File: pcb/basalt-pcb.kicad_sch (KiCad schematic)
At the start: 16 parts, among them J1 Conn_01x07_Pin, J2 Conn_01x07_Pin, J3 USB4215-03-A, J4 Conn_01x04_Pin, U1 DI78L3.3ZAB, U2 STM32C071F8Px

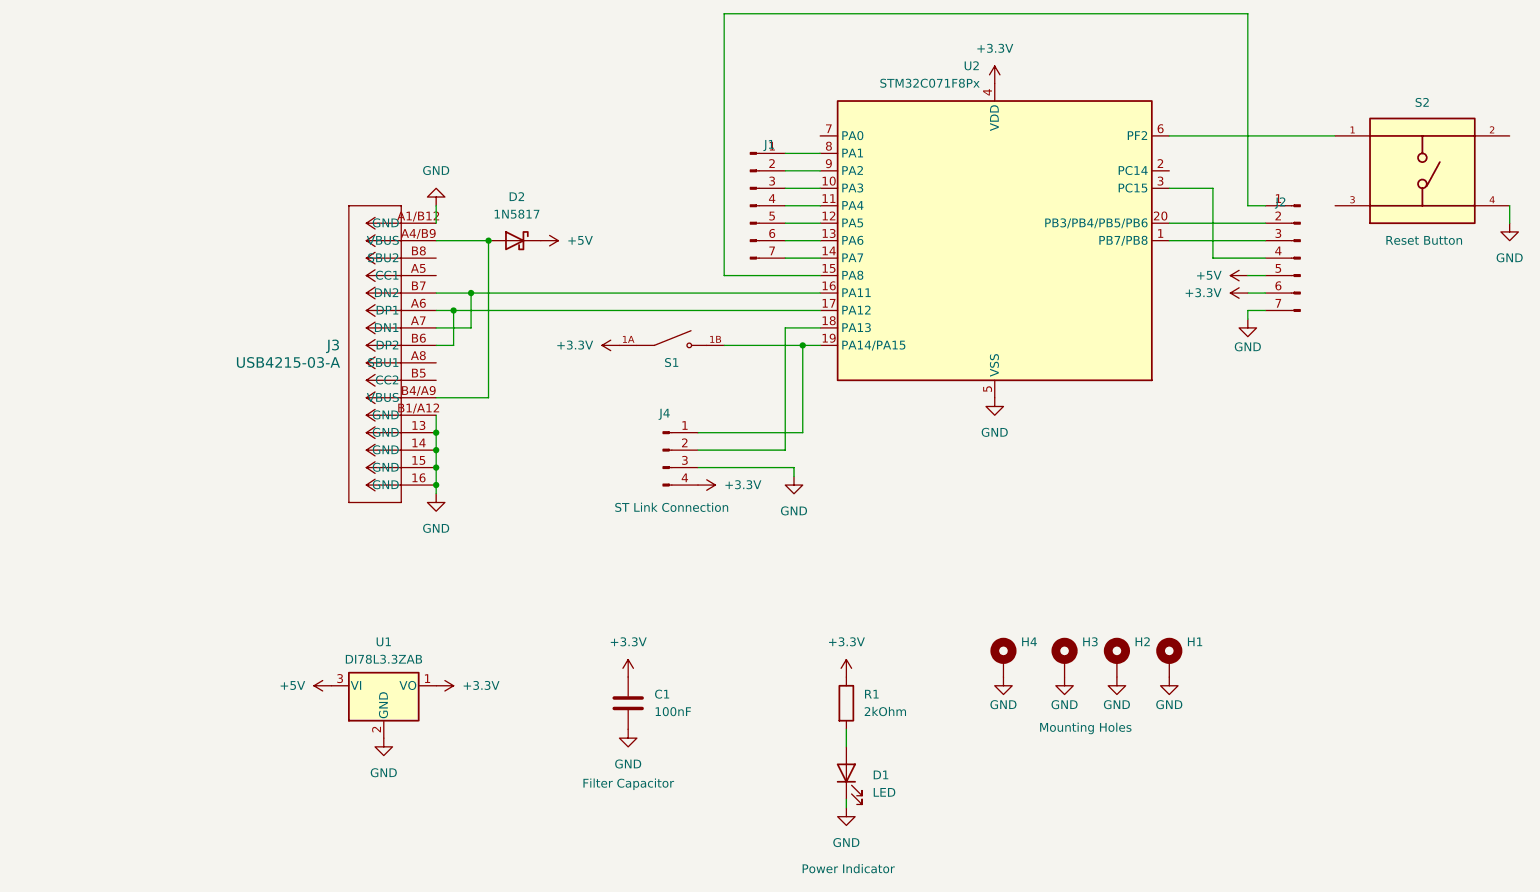
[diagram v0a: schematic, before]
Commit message: Begin work on Rev B with diode array / dedicated Vin pin
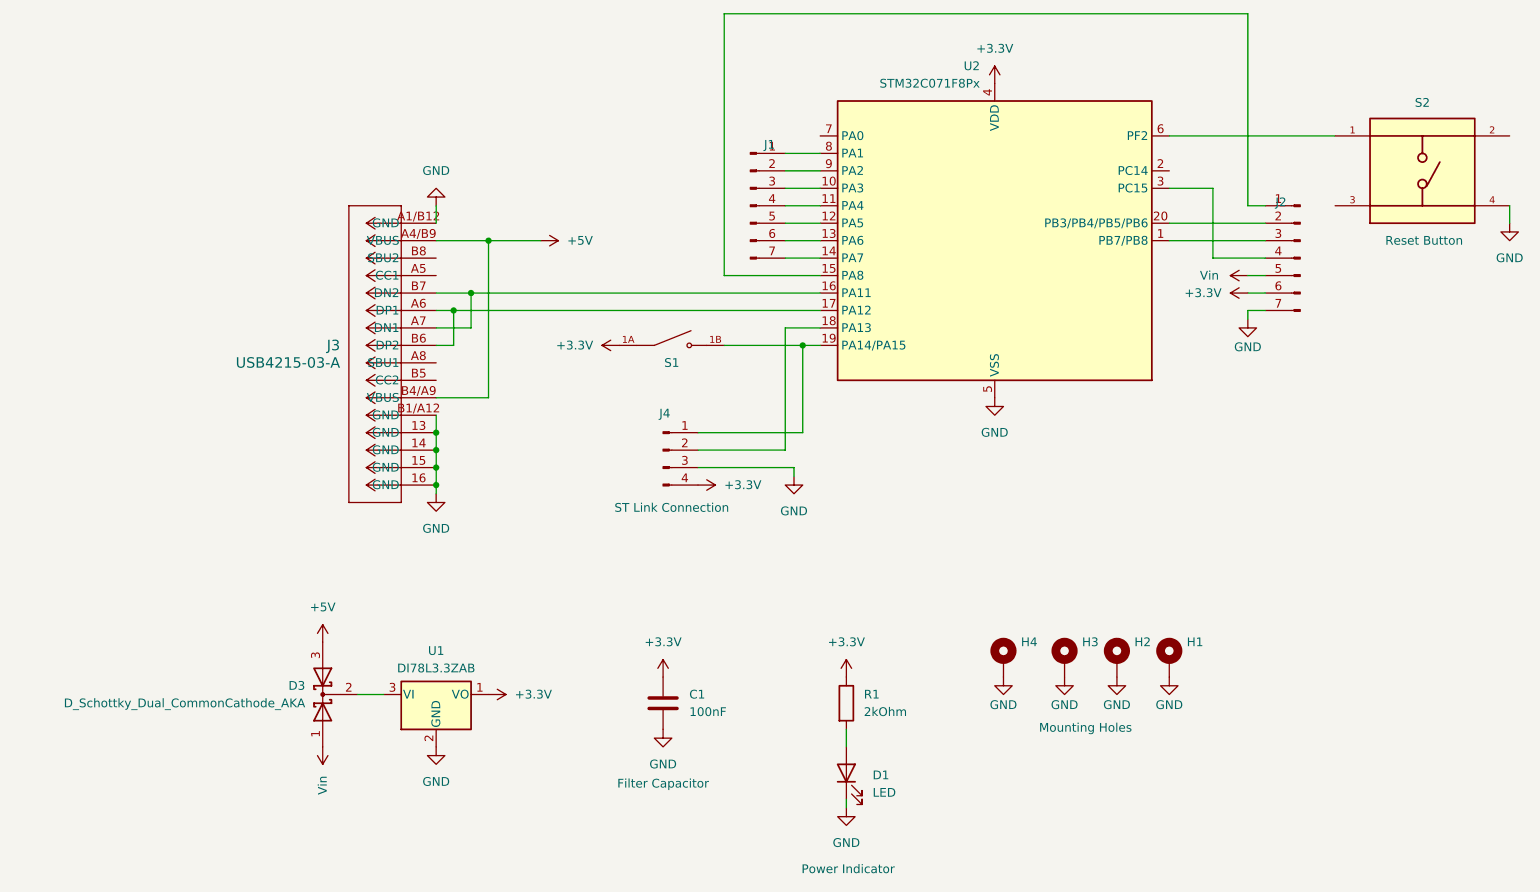
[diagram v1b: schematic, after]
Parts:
- removed D2: 1N5817, Diode_THT:D_DO-41_SOD81_P10.16mm_Horizontal, symbol Diode:1N5817
- added D3: D_Schottky_Dual_CommonCathode_AKA, Package_TO_SOT_THT:TO-220-3_Vertical, symbol Device:D_Schottky_Dual_CommonCathode_AKA
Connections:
- net +5V: now also J3.A4/B9 (VBUS), J3.B4/A9 (VBUS), D3.3 (A); no longer J2.5 (Pin_5), U1.3 (VI)
- new net: D3.2 (K), U1.3 (VI)
- new net Vin: D3.1 (A), J2.5 (Pin_5)
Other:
- moved on the sheet: C1, U1
